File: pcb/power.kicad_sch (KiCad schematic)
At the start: 6 parts, among them U3 LD39200PU33R

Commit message: buck converter and updates
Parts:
- added C41, C42: 10uF, Capacitor_SMD:C_0805_2012Metric, symbol Device:C_Small
- added C43, C44: 100nF, Capacitor_SMD:C_0402_1005Metric, symbol Device:C_Small
- added C45, C46, C47, C48: 22uF, Capacitor_SMD:C_0805_2012Metric, symbol Device:C_Small
- added C49: 1uF, Capacitor_SMD:C_0805_2012Metric, symbol Device:C_Small
- added C50: NC, Capacitor_SMD:C_0402_1005Metric, symbol Device:C_Small
- added C51: 22pF, Capacitor_SMD:C_0402_1005Metric, symbol Device:C_Small
- added L10: 1.5uH, Inductor_SMD:L_Coilcraft_XAL6030-XXX, symbol Device:L_Small
- added R1: 100k, Resistor_SMD:R_0603_1608Metric, symbol Device:R_Small
- added R13, R15: 0, Resistor_SMD:R_0603_1608Metric, symbol Device:R_Small
- added R14: 20k, Resistor_SMD:R_0603_1608Metric, symbol Device:R_Small
- added R2: 150k, Resistor_SMD:R_0603_1608Metric, symbol Device:R_Small
- added TP15: V_{IN}, TestPoint:TestPoint_Pad_2.0x2.0mm, symbol Connector:TestPoint
- added U8: TPS51386RJNR, footprints:VQFN-HR12_RJN_TEX, symbol TPS51386RJNR:TPS51386RJNR
- TP13: value V_{IN} -> 5V
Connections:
- net GND: now also C41.2, C42.2, C43.2, C45.2, C46.2, C47.2, C48.2, C49.2, C50.2, R14.1, U8.10 (AGND), U8.2 (PGND)
- net V_{IN}: now also C41.1, C42.1, C43.1, TP15.1, U8.1 (VIN); no longer C22.1, R5.1, TP13.1, U3.6 (IN)
- new net: C51.1, R13.2
- new net: C44.1, R15.2
- new net: C44.2, L10.1, U8.7 (SW)
- new net: R13.1, R14.2, R2.1, U8.4 (FB)
- new net: C50.1, U8.5 (SS)
- new net: R1.2, U8.3 (PG)
- new net: R15.1, U8.8 (VBST)
- new net: C49.1, R1.1, U8.9 (VCC)
- new net +5V: C22.1, C45.1, C46.1, C47.1, C48.1, C51.2, L10.2, R2.2, R5.1, TP13.1, U3.6 (IN)
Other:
- note added: "2S to 5V Buck Converter"
- note added: "5V to 3.3V LDO"
- note added: "V_{IN} is 2S [6V,8.4V] (7V Nominal)"
- moved on the sheet: C22, C23, R5, TP13, TP14, U3

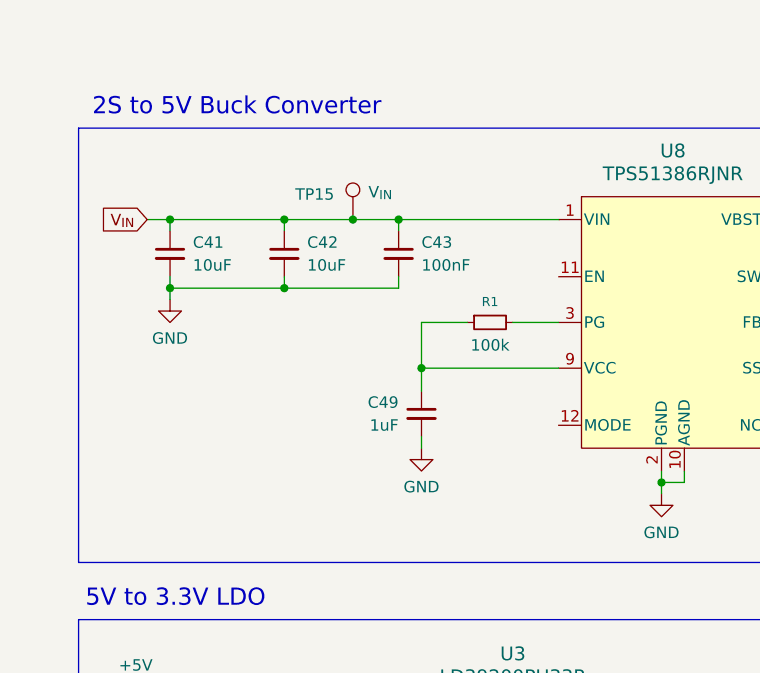
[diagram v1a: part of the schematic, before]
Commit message: switch TCXO, laid out from ref design from nordic
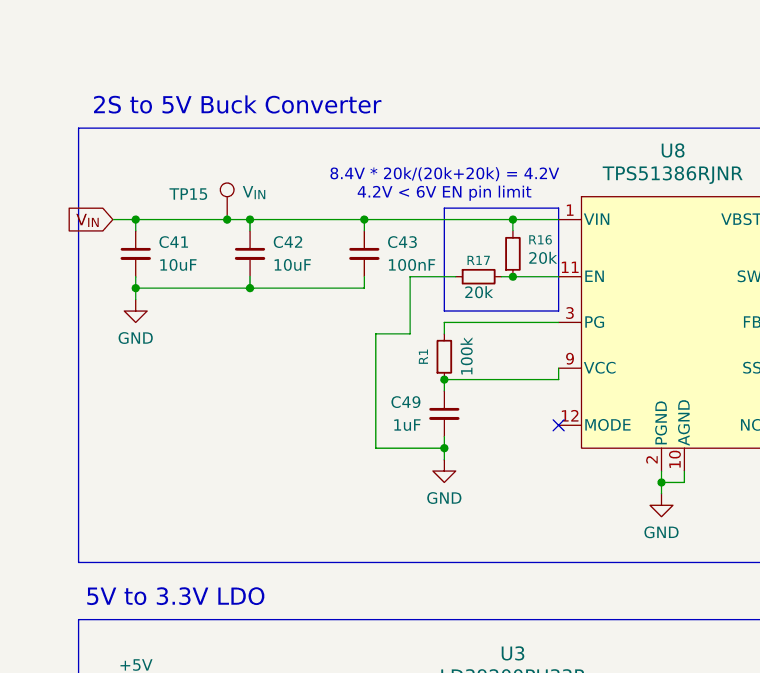
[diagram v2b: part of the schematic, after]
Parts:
- added R16, R17: 20k, Resistor_SMD:R_0603_1608Metric, symbol Device:R_Small
- C50: footprint Capacitor_SMD:C_0402_1005Metric -> Capacitor_SMD:C_0805_2012Metric
- U3: footprint footprint-lib:SON_DFN6_3X3_STM -> footprints:SON_DFN6_3X3_STM
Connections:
- net GND: now also R17.1
- net V_{IN}: now also R16.2
- net at U8.11 (EN): now also R16.1, R17.2
- no-connect marks 1 -> 2
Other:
- note added: "8.4V * 20k/(20k+20k) = 4.2V 4.2V < 6V EN pin limit"
- moved on the sheet: C41, C42, C43, C49, R1, TP15

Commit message: V2
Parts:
- TP5: renamed from TP15; footprint TestPoint:TestPoint_Pad_2.0x2.0mm -> TestPoint:TestPoint_Pad_D1.0mm
- TP6: renamed from TP13; footprint TestPoint:TestPoint_Pad_2.0x2.0mm -> TestPoint:TestPoint_Pad_D1.0mm
- TP7: renamed from TP14; footprint TestPoint:TestPoint_Pad_2.0x2.0mm -> TestPoint:TestPoint_Pad_D1.0mm
- renumbered C44 to C22, C41 to C23, C42 to C24, C43 to C25, C45 to C26, C46 to C27, C47 to C28, C48 to C29, C51 to C30, C50 to C31, C49 to C32, C23 to C33, C22 to C34, L10 to L5, R5 to R10, R15 to R3, R16 to R4, R17 to R5, R2 to R6, R1 to R7, R13 to R8, R14 to R9, U8 to U3, U3 to U4

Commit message: revision 3
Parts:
- added D1: Red, LED_SMD:LED_0603_1608Metric, symbol Device:LED_Small
- added D2, D3: DSS110U, Diode_SMD:D_SOD-123F, symbol Device:D_Schottky
- R3: value 0 -> 680
- R4, R5: value 20k -> 100k
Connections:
- net +3.3V: now also D1.2 (A)
- net +5V: now also D2.2 (A); no longer C34.1, R10.1, TP6.1, U4.6 (IN)
- net GND: now also R3.2
- net at C22.1: now also U3.8 (VBST); no longer R3.2
- net at R3.1: now also D1.1 (K); no longer U3.8 (VBST)
- new net: C34.1, D2.1 (K), D3.1 (K), R10.1, TP6.1, U4.6 (IN)
- new net VBUS: D3.2 (A)
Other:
- note added: "8.4V * 100k/(100k+100k) = 4.2V 4.2V < 6V EN pin limit"
- note removed: "8.4V * 20k/(20k+20k) = 4.2V 4.2V < 6V EN pin limit"
- moved on the sheet: C33, C34, R10, TP6, TP7, U4
